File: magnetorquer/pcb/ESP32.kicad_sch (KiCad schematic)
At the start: 1 part

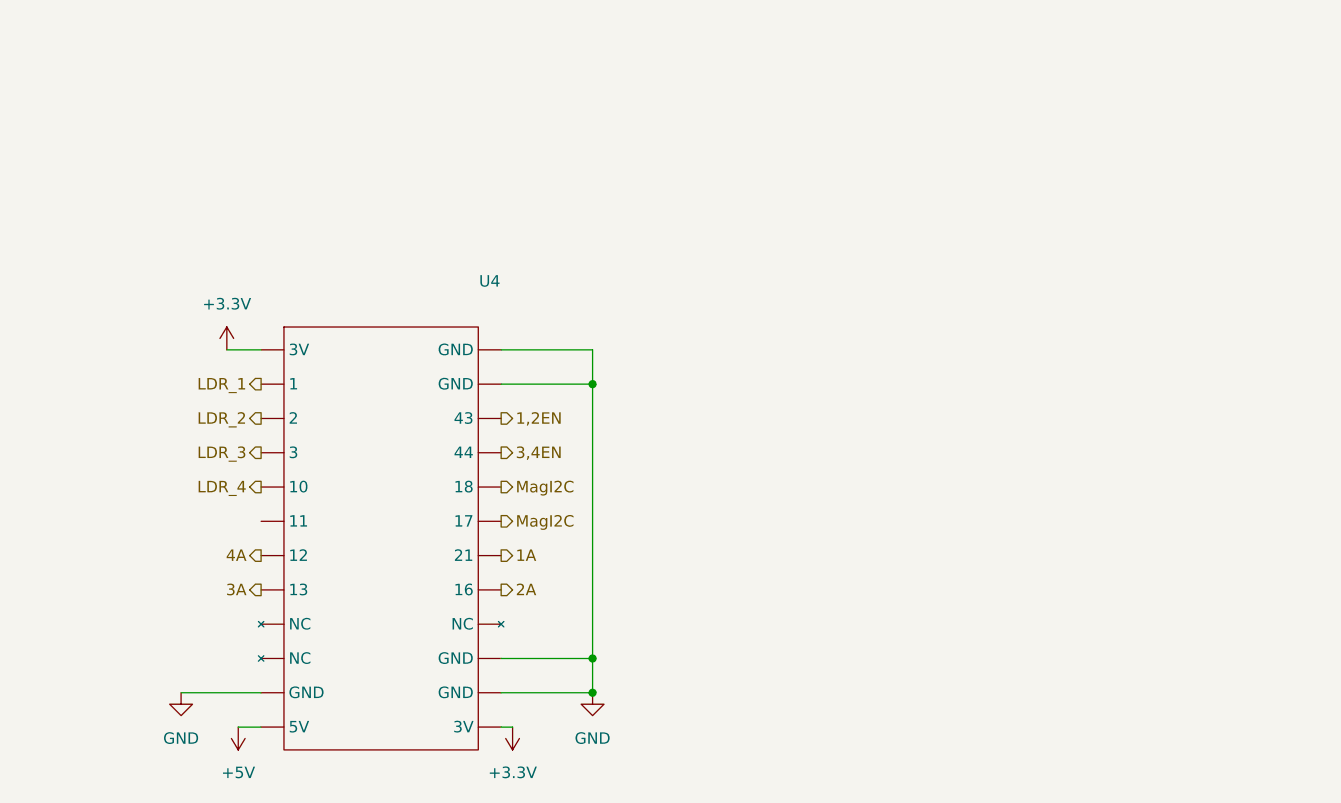
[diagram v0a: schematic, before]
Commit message: feat: lilygo s3 sch/footprint clean up sch
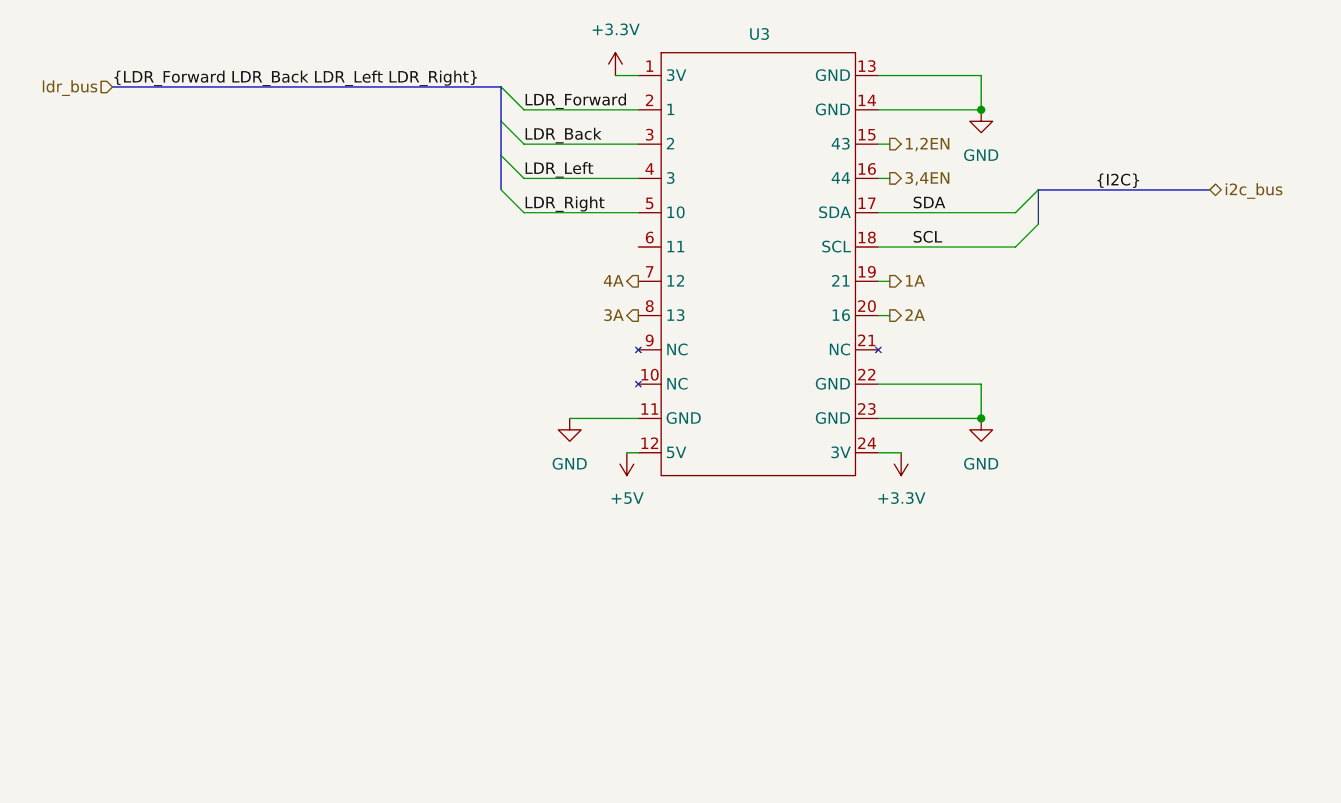
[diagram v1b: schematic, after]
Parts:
- removed U4: ~, symbol project_lib:EPS32_lilygo_s3
- added U3: ~, ESP32_boards:LILYGO_T-Display_ESP32-S3, symbol project_lib:LILYGO_T-Display_EPS32-s3
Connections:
- net +3.3V: now also U3.1 (3V), U3.24 (3V)
- net +5V: now also U3.12 (5V)
- net 1,2EN: now also U3.15 (43)
- net 1A: now also U3.19 (21)
- net 2A: now also U3.20 (16)
- net 3,4EN: now also U3.16 (44)
- net 3A: now also U3.8 (13)
- net 4A: now also U3.7 (12)
- net GND: now also U3.11 (GND), U3.13 (GND), U3.14 (GND), U3.22 (GND), U3.23 (GND)
- new net LDR_Back: U3.3 (2)
- new net LDR_Forward: U3.2 (1)
- new net LDR_Left: U3.4 (3)
- new net LDR_Right: U3.5 (10)
- new net SCL: U3.18 (17)
- new net SDA: U3.17 (18)

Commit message: start routing pcb
It needs a power regulator and a battery terminal
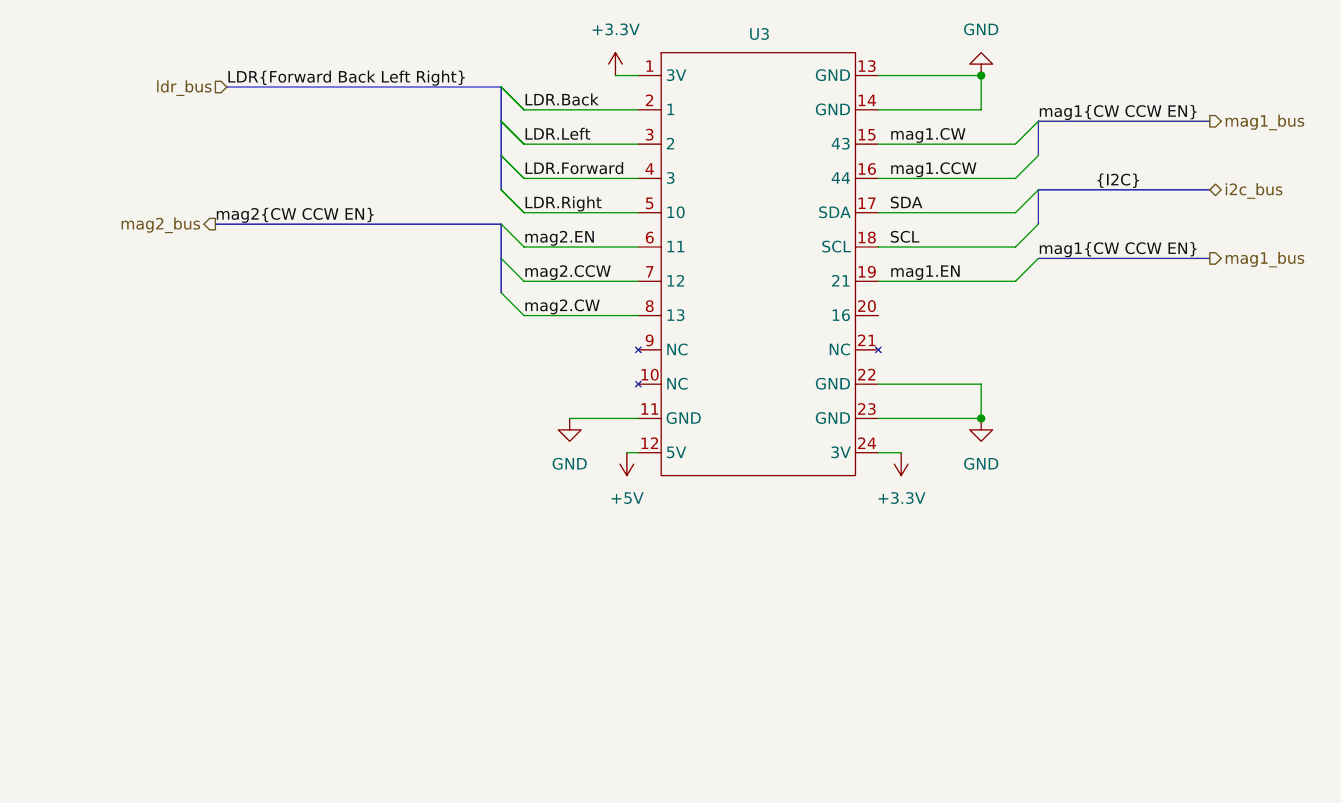
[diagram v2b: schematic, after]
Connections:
- net mag2.EN: now reaches U3.6 (11)
- net 1,2EN renamed mag1.CW
- net 1A renamed mag1.EN
- net 2A: no longer names the net of U3.20 (16)
- net 3,4EN renamed mag1.CCW
- net 3A renamed mag2.CW
- net 4A renamed mag2.CCW
- net LDR_Back renamed LDR.Left
- net LDR_Forward renamed LDR.Back
- net LDR_Left renamed LDR.Forward
- net LDR_Right renamed LDR.Right
